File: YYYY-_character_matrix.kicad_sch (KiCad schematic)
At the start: 14 parts, among them U15 SN74LVC244A, U16 SM411006N/15, U17 SM411006N/15, U18 SN74LVC244A, U19 SM411006N/15, U20 SM411006N/15, U21 SM411006N/15

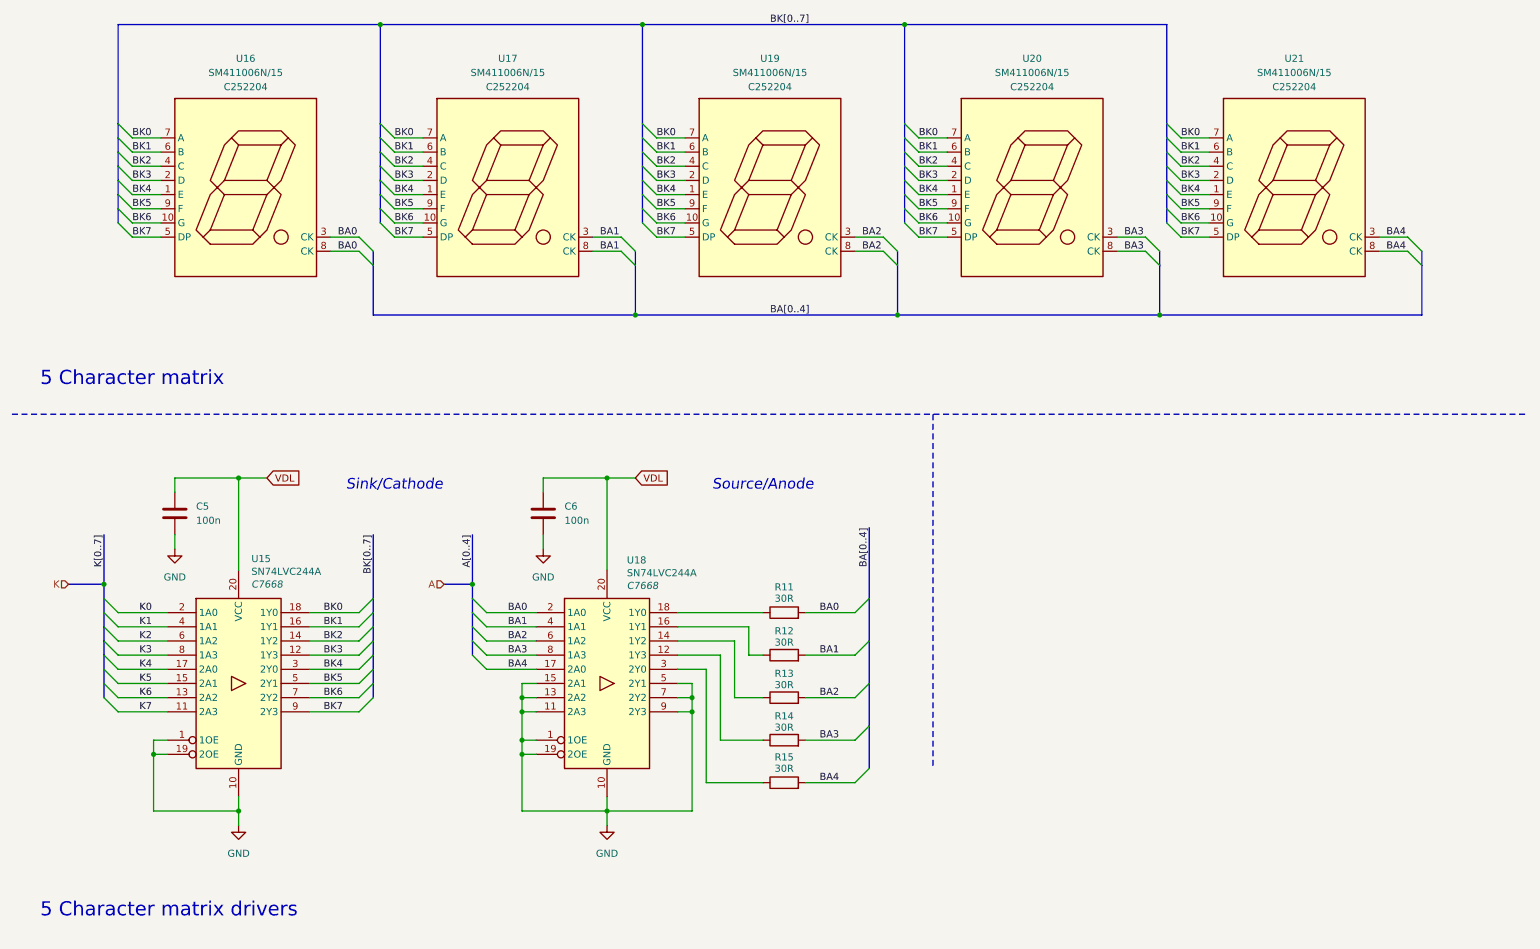
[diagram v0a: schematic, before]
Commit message: addition of bus
- cleaned up the structure of the schematic.
- addition of the colon
- root schematic improvements
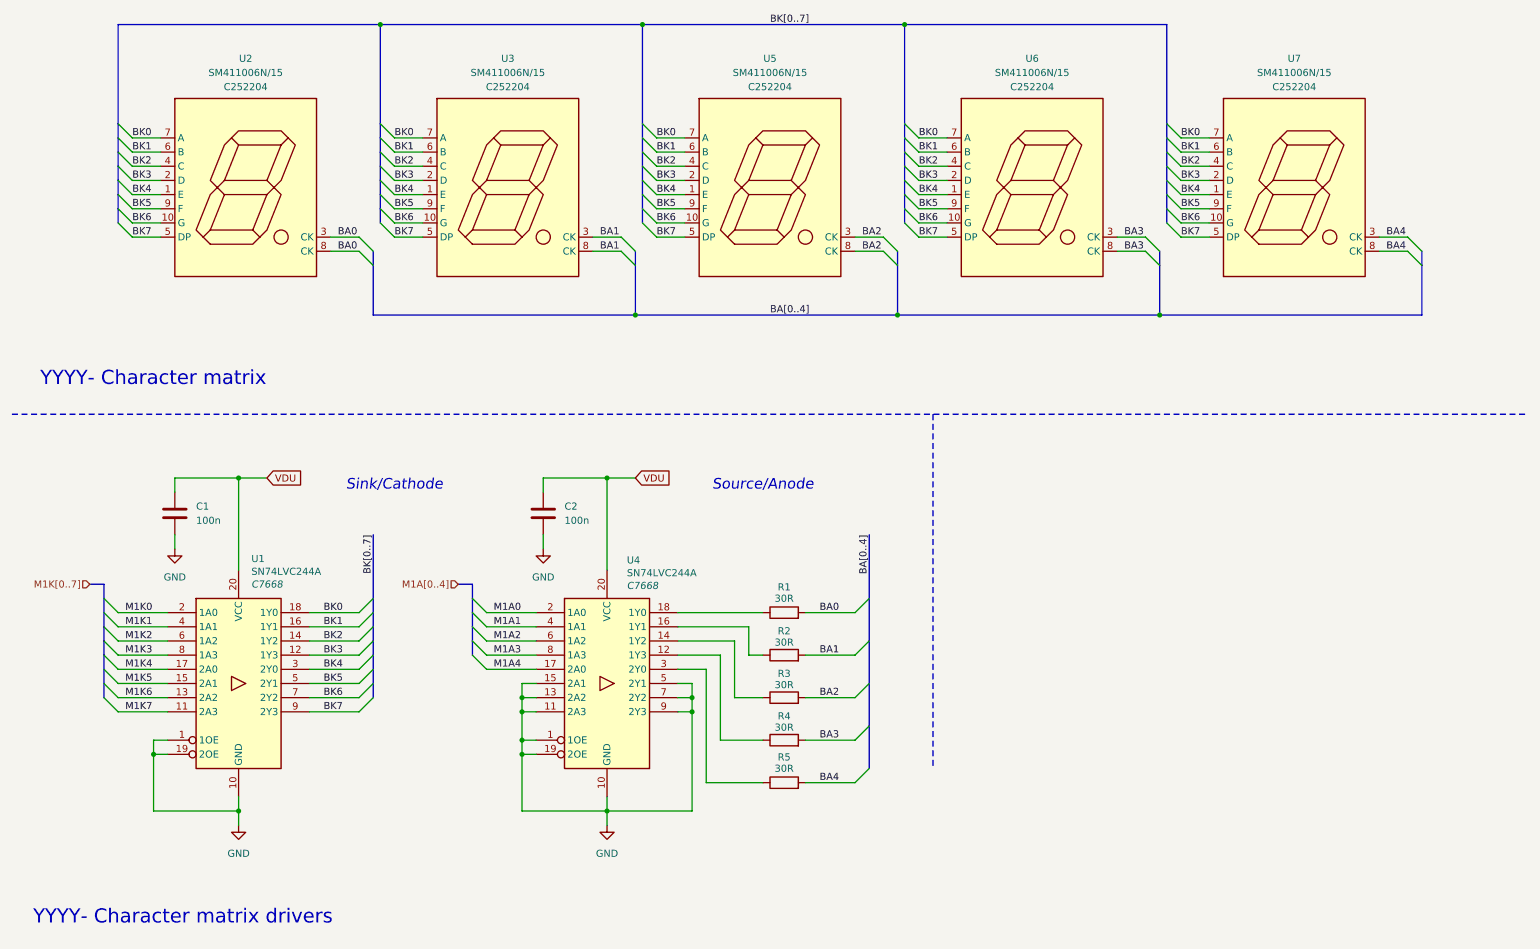
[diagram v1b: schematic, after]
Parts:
- removed C5, C6: 100n, symbol Device:C
- removed R11, R12, R13, R14, R15: 30R, symbol Device:R
- removed U15, U18: SN74LVC244A, Package_SO:TSSOP-20_4.4x6.5mm_P0.65mm, symbol 74xx:74AHC244
- removed U16, U17, U19, U20, U21: SM411006N/15, precision_clock:SM411006N15, symbol precision_clock:SM411006N/15
- added C1, C2: 100n, symbol Device:C
- added R1, R2, R3, R4, R5: 30R, symbol Device:R
- added U1, U4: SN74LVC244A, Package_SO:TSSOP-20_4.4x6.5mm_P0.65mm, symbol 74xx:74AHC244
- added U2, U3, U5, U6, U7: SM411006N/15, precision_clock:SM411006N15, symbol precision_clock:SM411006N/15
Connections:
- net BA0: now also R1.2, U2.3 (CK), U2.8 (CK)
- net BA1: now also R2.2, U3.3 (CK), U3.8 (CK)
- net BA2: now also R3.2, U5.3 (CK), U5.8 (CK)
- net BA3: now also R4.2, U6.3 (CK), U6.8 (CK)
- net BA4: now also R5.2, U7.3 (CK), U7.8 (CK)
- net BK0: now also U1.18 (1Y0), U2.7 (A), U3.7 (A), U5.7 (A), U6.7 (A), U7.7 (A)
- net BK1: now also U1.16 (1Y1), U2.6 (B), U3.6 (B), U5.6 (B), U6.6 (B), U7.6 (B)
- net BK2: now also U1.14 (1Y2), U2.4 (C), U3.4 (C), U5.4 (C), U6.4 (C), U7.4 (C)
- net BK3: now also U1.12 (1Y3), U2.2 (D), U3.2 (D), U5.2 (D), U6.2 (D), U7.2 (D)
- net BK4: now also U1.3 (2Y0), U2.1 (E), U3.1 (E), U5.1 (E), U6.1 (E), U7.1 (E)
- net BK5: now also U1.5 (2Y1), U2.9 (F), U3.9 (F), U5.9 (F), U6.9 (F), U7.9 (F)
- net BK6: now also U1.7 (2Y2), U2.10 (G), U3.10 (G), U5.10 (G), U6.10 (G), U7.10 (G)
- net BK7: now also U1.9 (2Y3), U2.5 (DP), U3.5 (DP), U5.5 (DP), U6.5 (DP), U7.5 (DP)
- net GND: now also C1.2, C2.2, U1.1 (1OE), U1.10 (GND), U1.19 (2OE), U4.1 (1OE), U4.10 (GND), U4.11 (2A3), U4.13 (2A2), U4.15 (2A1), U4.19 (2OE), U4.5 (2Y1), U4.7 (2Y2), U4.9 (2Y3)
- new net: R3.1, U4.14 (1Y2)
- new net: R4.1, U4.12 (1Y3)
- new net: R2.1, U4.16 (1Y1)
- new net: R1.1, U4.18 (1Y0)
- new net: R5.1, U4.3 (2Y0)
- new net M1A0: U4.2 (1A0)
- new net M1A1: U4.4 (1A1)
- new net M1A2: U4.6 (1A2)
- new net M1A3: U4.8 (1A3)
- new net M1A4: U4.17 (2A0)
- new net M1K0: U1.2 (1A0)
- new net M1K1: U1.4 (1A1)
- new net M1K2: U1.6 (1A2)
- new net M1K3: U1.8 (1A3)
- new net M1K4: U1.17 (2A0)
- new net M1K5: U1.15 (2A1)
- new net M1K6: U1.13 (2A2)
- new net M1K7: U1.11 (2A3)
- new net VDU: C1.1, C2.1, U1.20 (VCC), U4.20 (VCC)
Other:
- note added: "YYYY- Character matrix"
- note added: "YYYY- Character matrix drivers"
- note removed: "5 Character matrix"
- note removed: "5 Character matrix drivers"
- title: 5 Character Matrix & Drivers  -> YYYY- Character Matrix & Drivers 

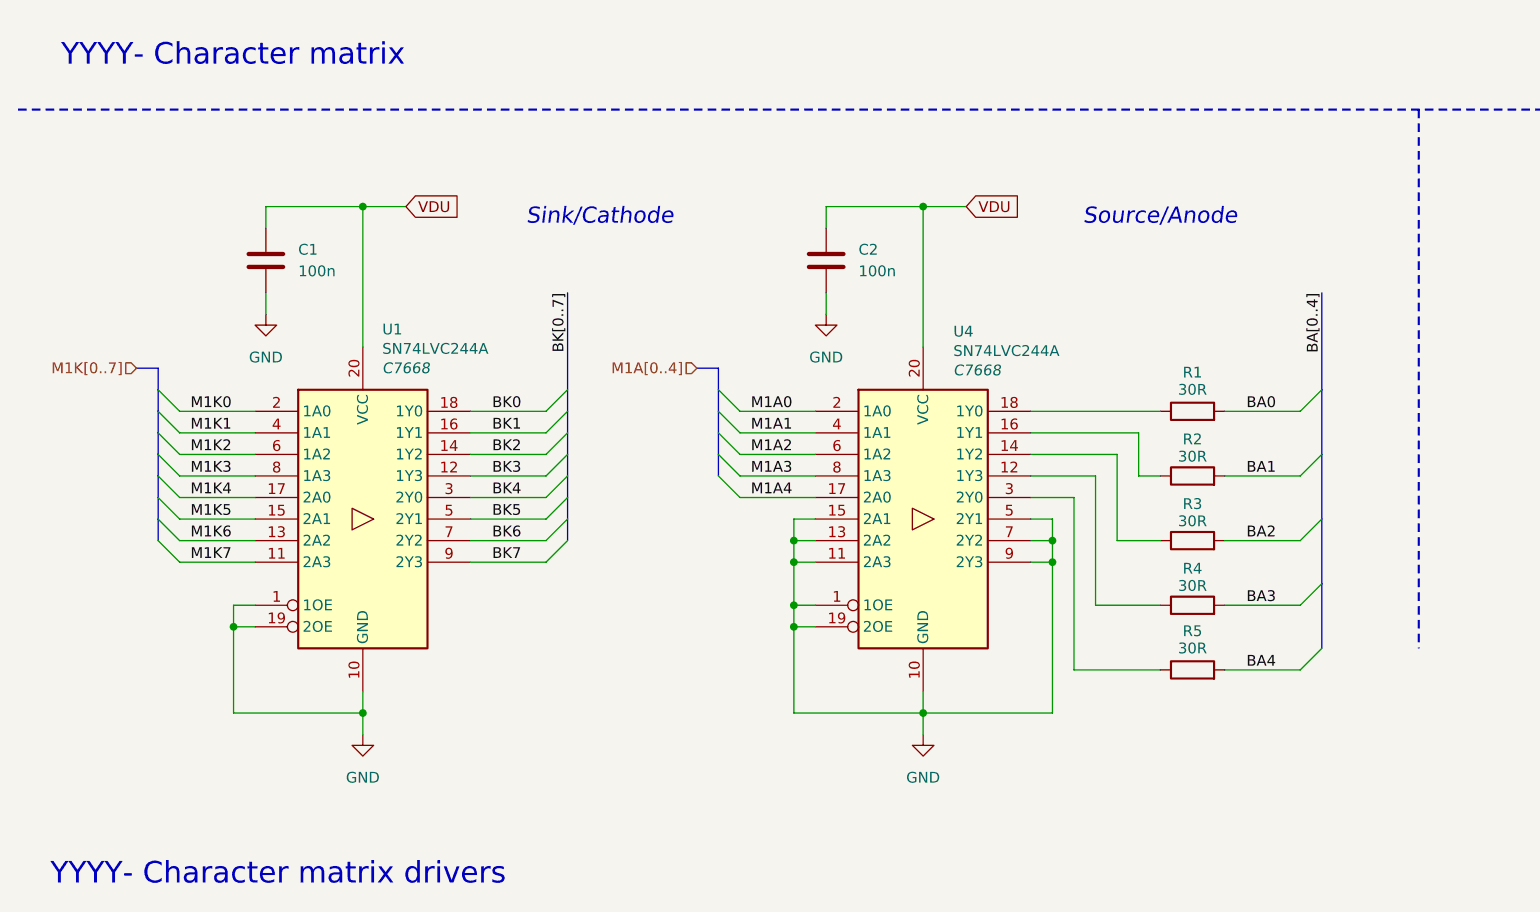
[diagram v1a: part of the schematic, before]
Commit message: current limiting resistor changes
- added colon led model, but might replace it in the future.
- reduction in current limiting resistance.
- removed the solder jumps in the individual circuit schematics.
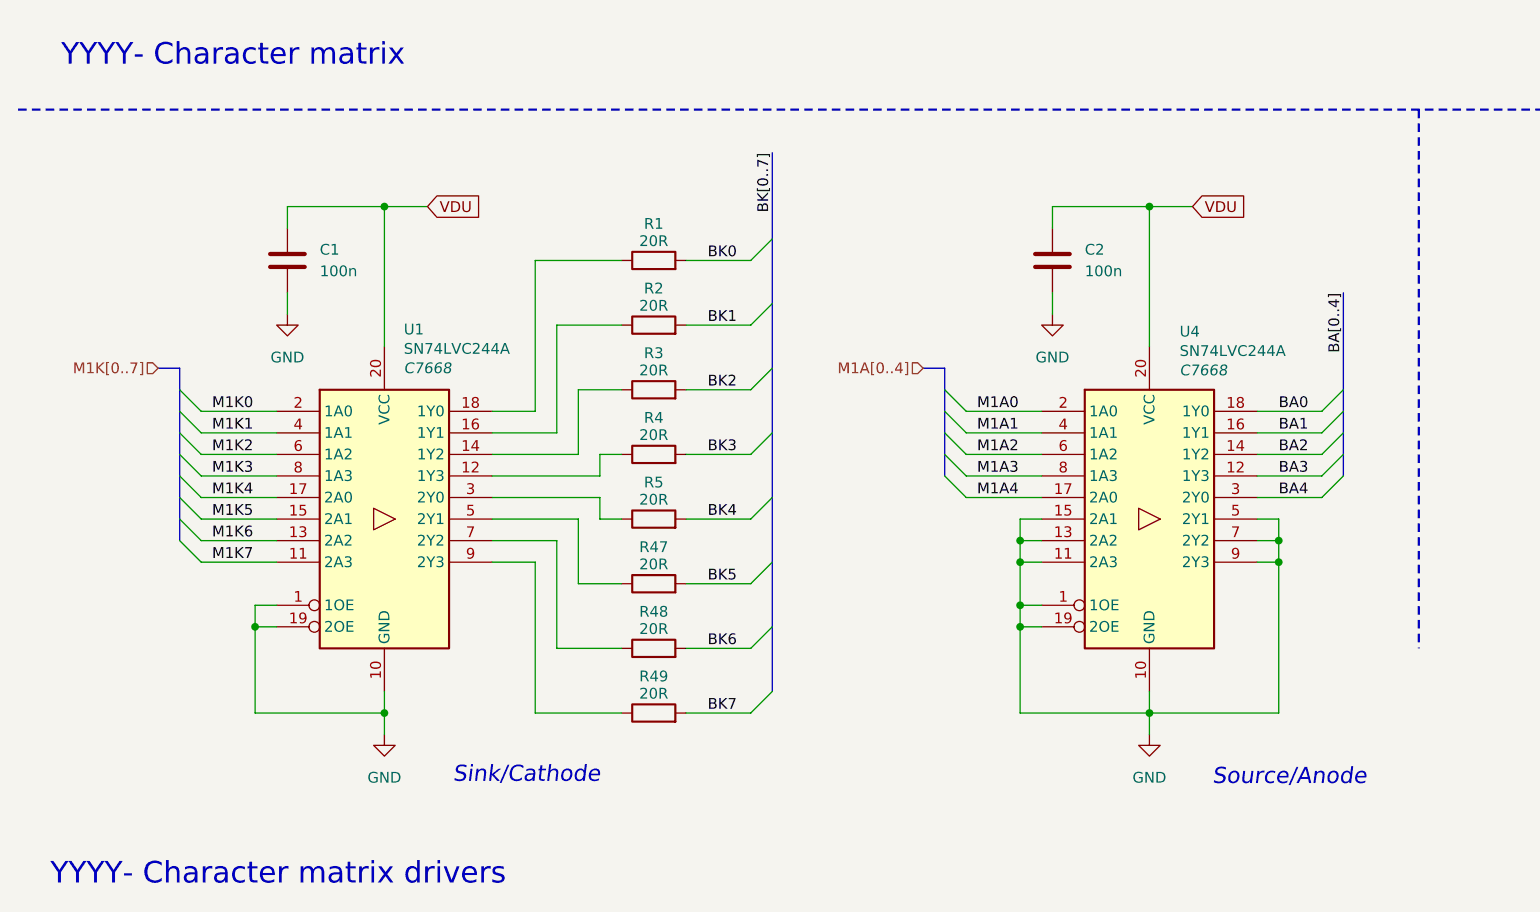
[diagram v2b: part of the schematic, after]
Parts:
- added R47, R48, R49: 20R, symbol Device:R
- R1, R2, R3, R4, R5: value 30R -> 20R
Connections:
- net BA0: now also U4.18 (1Y0); no longer R1.2
- net BA1: now also U4.16 (1Y1); no longer R2.2
- net BA2: now also U4.14 (1Y2); no longer R3.2
- net BA3: now also U4.12 (1Y3); no longer R4.2
- net BA4: now also U4.3 (2Y0); no longer R5.2
- net BK0: now also R1.2; no longer U1.18 (1Y0)
- net BK1: now also R2.2; no longer U1.16 (1Y1)
- net BK2: now also R3.2; no longer U1.14 (1Y2)
- net BK3: now also R4.2; no longer U1.12 (1Y3)
- net BK4: now also R5.2; no longer U1.3 (2Y0)
- net BK5: now also R47.2; no longer U1.5 (2Y1)
- net BK6: now also R48.2; no longer U1.7 (2Y2)
- net BK7: now also R49.2; no longer U1.9 (2Y3)
- net at R3.1: now also U1.14 (1Y2); no longer U4.14 (1Y2)
- net at R4.1: now also U1.12 (1Y3); no longer U4.12 (1Y3)
- net at R2.1: now also U1.16 (1Y1); no longer U4.16 (1Y1)
- net at R1.1: now also U1.18 (1Y0); no longer U4.18 (1Y0)
- net at R5.1: now also U1.3 (2Y0); no longer U4.3 (2Y0)
- new net: R47.1, U1.5 (2Y1)
- new net: R48.1, U1.7 (2Y2)
- new net: R49.1, U1.9 (2Y3)

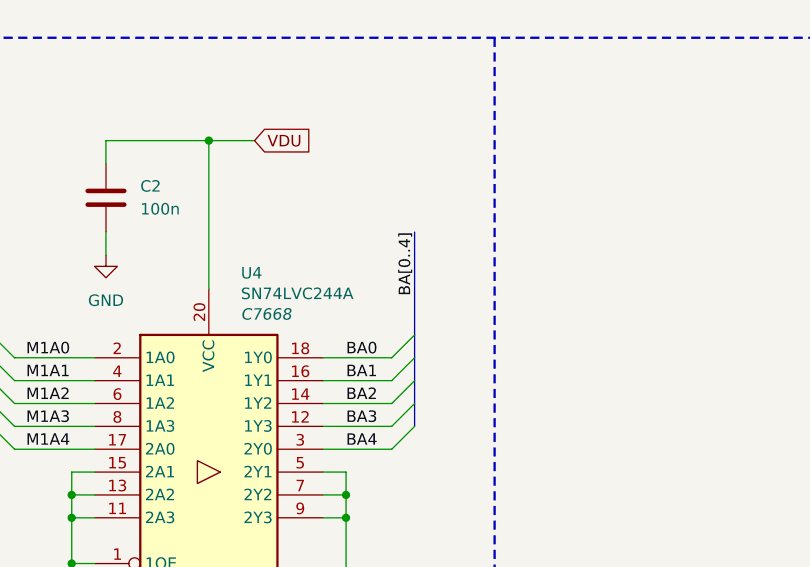
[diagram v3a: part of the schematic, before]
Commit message: Buzzer driver added - replacement of photoresistor to a variable resistor - added button - general formatting
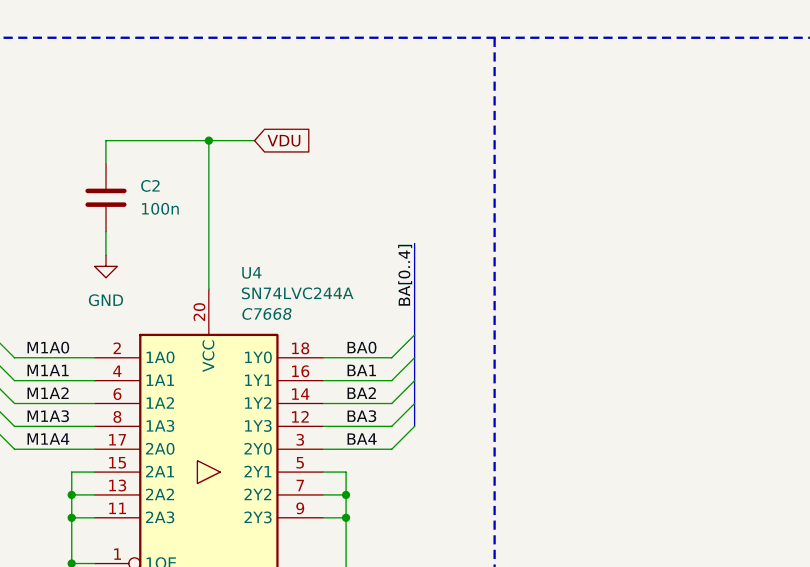
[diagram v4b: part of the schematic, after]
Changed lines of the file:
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@@
 	(bus
 		(pts
-			(xy 168.91 123.19) (xy 168.91 134.62)
+			(xy 168.91 124.46) (xy 168.91 134.62)
 		)
 		(stroke
@@
 	)
 	(label "BA[0..4]"
-		(at 168.91 123.19 270)
-		(effects
-			(font
+		(at 168.91 124.46 270)
+		(effects
+			(font

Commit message: ESD, LEDs, footprints
- assignment of footprints
- ESD protection
- User buttons
- addition of test points
- BOM consolidation of  resistors
- general reordering of the schematic
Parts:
- C1, C2: footprint (none) -> Capacitor_SMD:C_0603_1608Metric
- R1, R2, R3, R4, R47, R48, R49, R5: footprint (none) -> Resistor_SMD:R_0603_1608Metric
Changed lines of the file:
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@@
 	(title_block
 		(title "YYYY- Character Matrix & Drivers ")
-		(date "2025-10-31")
+		(date "2025-11-04")
 		(rev "v0.0")
 		(company "Rajath Katker")
@@
 			)
 		)
-		(property "Footprint" ""
+		(property "Footprint" "Resistor_SMD:R_0603_1608Metric"
 			(at 87.63 121.158 90)
 			(effects
@@
 			)
 		)
-		(property "Footprint" ""
+		(property "Footprint" "Resistor_SMD:R_0603_1608Metric"
 			(at 87.63 136.398 90)
 			(effects
@@
 			)
 		)
-		(property "Footprint" ""
+		(property "Footprint" "Capacitor_SMD:C_0603_1608Metric"
 			(at 135.5852 123.19 0)
 			(effects
@@
 			)
 		)
-		(property "Footprint" ""
+		(property "Footprint" "Resistor_SMD:R_0603_1608Metric"
 			(at 87.63 144.018 90)
 			(effects
@@
 			)
 		)
-		(property "Footprint" ""
+		(property "Footprint" "Resistor_SMD:R_0603_1608Metric"
 			(at 87.63 159.258 90)
 			(effects
@@
 			)
 		)
-		(property "Footprint" ""
+		(property "Footprint" "Capacitor_SMD:C_0603_1608Metric"
 			(at 45.4152 123.19 0)
 			(effects
@@
 			)
 		)
-		(property "Footprint" ""
+		(property "Footprint" "Resistor_SMD:R_0603_1608Metric"
 			(at 87.63 166.878 90)
 			(effects
@@
 			)
 		)
-		(property "Footprint" ""
+		(property "Footprint" "Resistor_SMD:R_0603_1608Metric"
 			(at 87.63 128.778 90)
 			(effects
@@
 			)
 		)
-		(property "Footprint" ""
+		(property "Footprint" "Resistor_SMD:R_0603_1608Metric"
 			(at 87.63 151.638 90)
 			(effects
@@
 			)
 		)
-		(property "Footprint" ""
+		(property "Footprint" "Resistor_SMD:R_0603_1608Metric"
 			(at 87.63 174.498 90)
 			(effects
